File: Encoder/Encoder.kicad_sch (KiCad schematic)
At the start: 60 parts, among them J1 Conn_01x02_Male, J2 Conn_01x04_Male, J3 Conn_01x04_Male, J4 Conn_01x04_Female, Q1 SSM3J332R, Q12 S8050, Q2 BSS138, Q3 SSM3J332R, SW1 SW_DIP_x05, SW2 SW_SPDT_White, SW3 SW_SPST, U1 AZ1084CD-3.3, U2 MAX3485, U3 AS5600, U4 STM32C011F4P6, Y1 48MHz

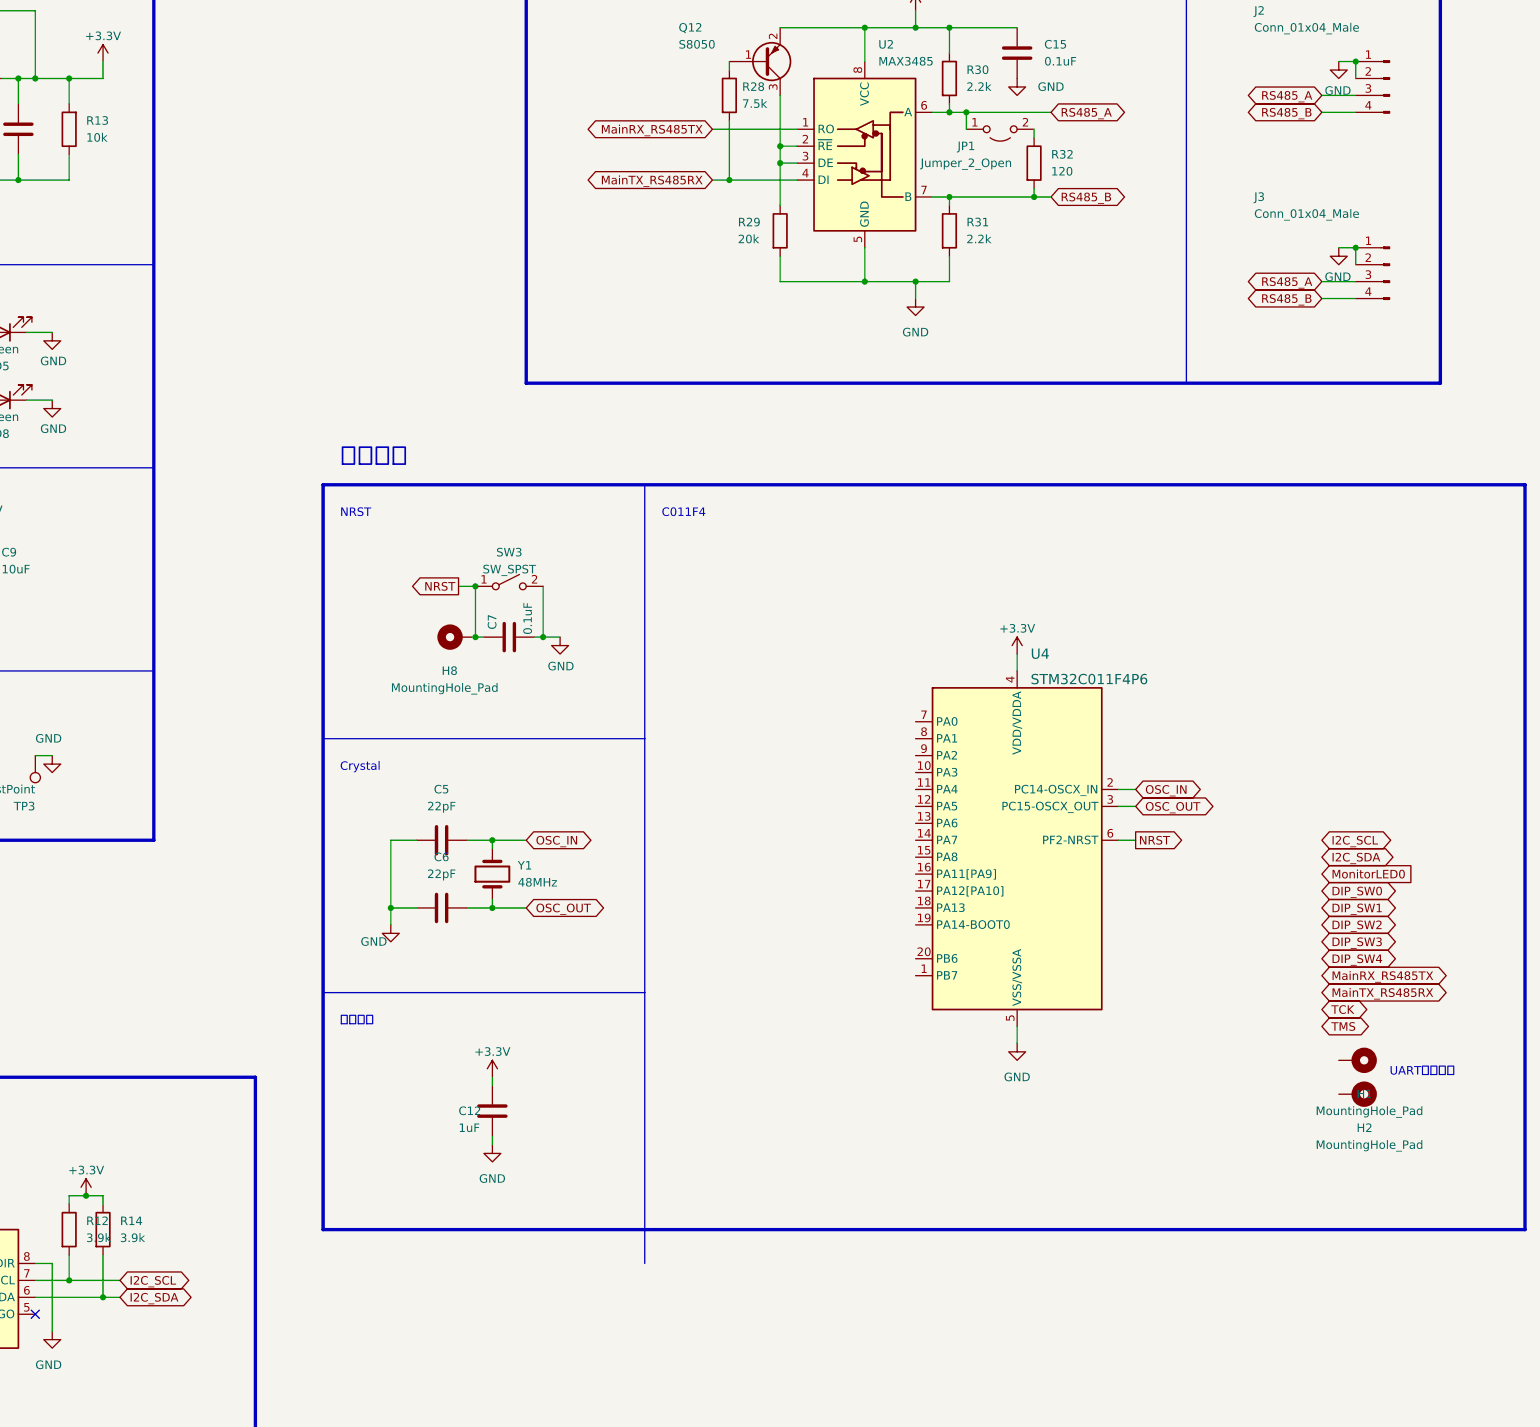
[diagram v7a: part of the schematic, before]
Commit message: エンコーダー基板配線完了
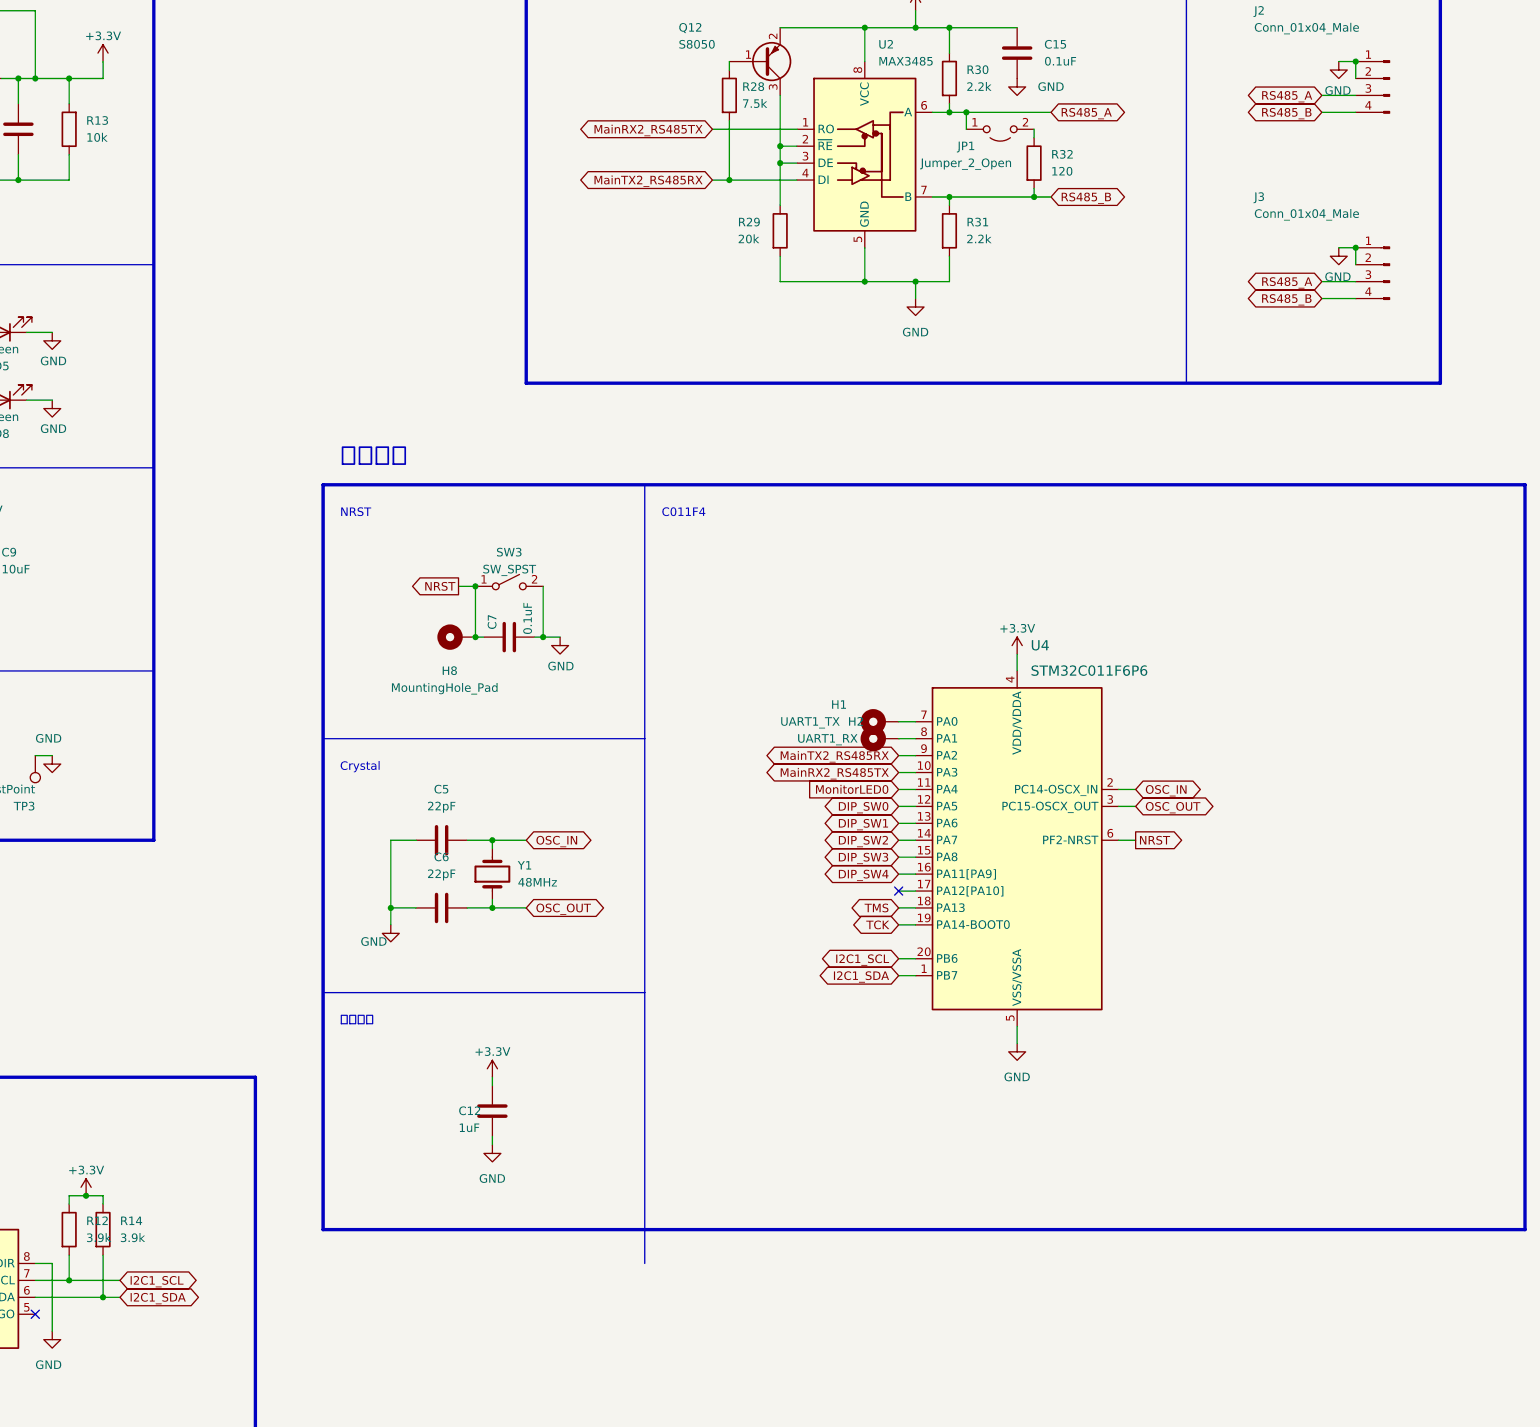
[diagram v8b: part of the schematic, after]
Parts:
- H1: value MountingHole_Pad -> UART1_TX
- H2: value MountingHole_Pad -> UART1_RX
- U4: value STM32C011F4P6 -> STM32C011F6P6
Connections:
- net I2C_SCL is gone; now on net I2C1_SCL: R12.2, U3.7 (SCL)
- net I2C_SDA is gone; now on net I2C1_SDA: R14.2, U3.6 (SDA)
- net MainRX_RS485TX is gone; now on net MainRX2_RS485TX: U2.1 (RO)
- net MainTX_RS485RX is gone; now on net MainTX2_RS485RX: R28.2, U2.4 (DI)
- net DIP_SW0: now also U4.12 (PA5)
- net DIP_SW1: now also U4.13 (PA6)
- net DIP_SW2: now also U4.14 (PA7)
- net DIP_SW3: now also U4.15 (PA8)
- net DIP_SW4: now also U4.16 (PA11[PA9])
- net MonitorLED0: now also U4.11 (PA4)
- net TCK: now also U4.19 (PA14-BOOT0)
- net TMS: now also U4.18 (PA13)
- net I2C1_SDA: now reaches U4.1 (PB7)
- net MainRX2_RS485TX: now reaches U4.10 (PA3)
- net I2C1_SCL: now reaches U4.20 (PB6)
- net at U4.7 (PA0): now also H1.1
- net at U4.8 (PA1): now also H2.1
- net MainTX2_RS485RX: now reaches U4.9 (PA2)
- no-connect marks 3 -> 4
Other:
- note removed: "UART引き出す"
- moved on the sheet: H1, H2
